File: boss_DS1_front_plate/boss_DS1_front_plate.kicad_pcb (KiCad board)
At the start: 2 copper layers, 80 x 100 mm, 16 parts

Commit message: Updated front.
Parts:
- added D1: LED, pedale:red_led, F.Cu at (74.0, 138.0)
- added D2: LED, pedale:green_led, F.Cu at (106.0, 138.0)
- added J1: top_panel_connector, pedale:bottom_connector, B.Cu at (80.5, 102.8)
- added RV1: R_Potentiometer, pedale:top_plate_pot, F.Cu at (68.0, 63.0)
- added RV2: R_Potentiometer, pedale:top_plate_pot, F.Cu at (112.0, 63.0)
- added RV3: R_Potentiometer, pedale:top_plate_pot, F.Cu at (90.0, 78.0)

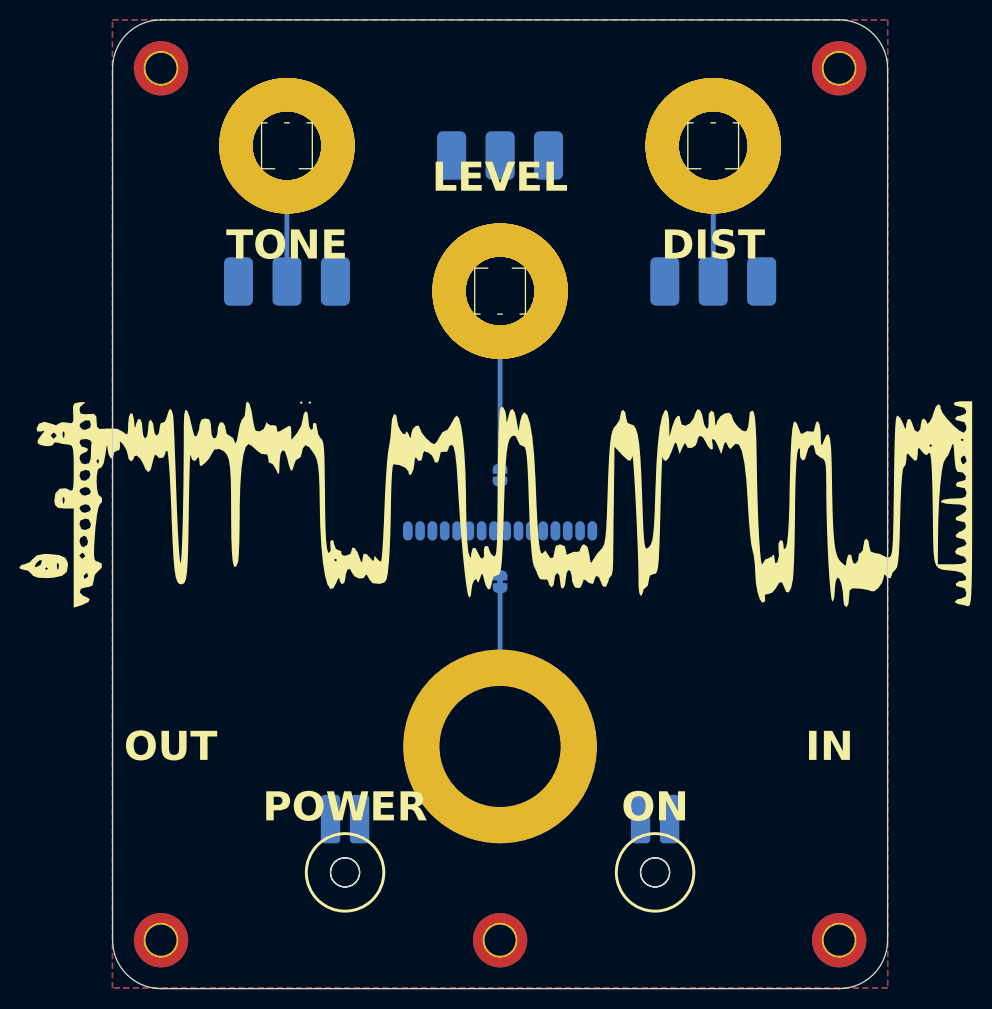
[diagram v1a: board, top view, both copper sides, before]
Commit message: Potentiometers checked.
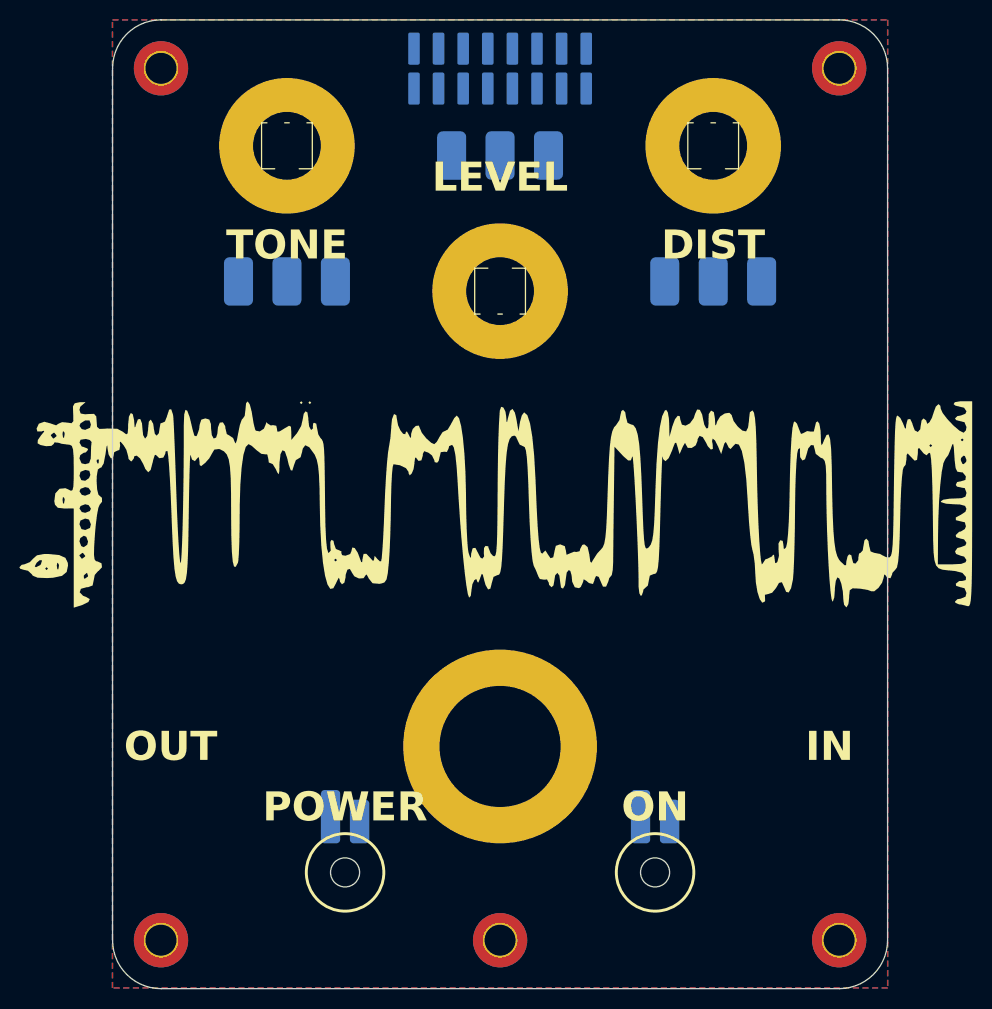
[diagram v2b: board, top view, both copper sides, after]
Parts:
- removed H10, H9: MountingHole, MountingHole:MountingHole_3mm
- removed H5, H6, H7: MountingHole_Pad, pedale:plated_pot_hole
- removed JP1, JP2, JP3, JP4: SolderJumper_2_Bridged, Jumper:SolderJumper-2_P1.3mm_Bridged_RoundedPad1.0x1.5mm
- J1: footprint pedale:bottom_connector -> pedale:IDC-Header_2x08_faux_SMD
- RV1, RV2, RV3: value R_Potentiometer -> pot_gnd
- moved J1 49.0 mm to (81.1, 53.7)
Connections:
- H8 pad 1: Net-(JP4-B) -> 0
- J1 pad 3: unconnected-(J1F-GND-Pad3) -> 0
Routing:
- net Net-(JP2-B): track 18.3 -> 0.00 mm
- net Net-(JP4-B): track 16.3 -> 0.00 mm
- net Net-(JP3-B): track 12.3 -> 0.00 mm
- net Net-(JP1-B): track 12.3 -> 0.00 mm

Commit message: Pots again, done.
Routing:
- net Net-(J1A-Pin_2): track 0.00 -> 29.5 mm
- net Net-(J1A-Pin_4): track 0.00 -> 26.4 mm
- net Net-(J1A-Pin_6): track 0.00 -> 25.4 mm
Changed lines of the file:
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@@
 	)
 	(footprint "pedale:top_plate_pot"
+		(locked yes)
 		(layer "F.Cu")
 		(at 90 78 180)
@@
 	)
 	(footprint "pedale:green_led"
+		(locked yes)
 		(layer "F.Cu")
 		(at 106 138 180)
@@
 	)
 	(footprint "pedale:top_plate_pot"
+		(locked yes)
 		(layer "F.Cu")
 		(at 112 63)
@@
 	)
 	(footprint "pedale:top_plate_pot"
+		(locked yes)
 		(layer "F.Cu")
 		(at 68 63)
@@
 	)
 	(footprint "LOGO"
+		(locked yes)
 		(layer "F.Cu")
 		(at 90 100)
@@
 	)
 	(footprint "pedale:red_led"
+		(locked yes)
 		(layer "F.Cu")
 		(at 74 138 180)
@@
 	)
 	(gr_text "IN"
+		(locked yes)
 		(at 124 125 0)
 		(layer "F.SilkS")
@@
 	)
 	(gr_text "POWER\n"
+		(locked yes)
 		(at 74 133 0)
 		(layer "F.SilkS")
@@
 	)
 	(gr_text "OUT\n"
+		(locked yes)
 		(at 56 125 0)
 		(layer "F.SilkS")
@@
 	)
 	(gr_text "ON\n"
+		(locked yes)
 		(at 106 133 0)
 		(layer "F.SilkS")
@@
 		)
 	)
+	(segment
+		(start 79.1 63.297499)
+		(end 79.1 64.7)
+		(width 0.5)
+		(layer "B.Cu")
+		(net 7)
+	)
+	(segment
+		(start 68 75.8)
+		(end 68 77)
+		(width 0.5)
+		(layer "B.Cu")
+		(net 7)
+	)
+	(segment
+		(start 79.1 64.7)
+		(end 68 75.8)
+		(width 0.5)
+		(layer "B.Cu")
+		(net 7)
+	)
+	(segment
+		(start 83.65 58.747499)
+		(end 79.1 63.297499)
+		(width 0.5)
+		(layer "B.Cu")
+		(net 7)
+	)
+	(segment
+		(start 83.65 57.0925)
+		(end 83.65 58.747499)
+		(width 0.5)
+		(layer "B.Cu")
+		(net 7)
+	)
+	(segment
+		(start 86.19 57.0925)
+		(end 86.19 58.11)
+		(width 0.5)
+		(layer "B.Cu")
+		(net 12)
+	)
+	(segment
+		(start 86.19 58.11)
+		(end 80.8 63.5)
+		(width 0.5)
+		(layer "B.Cu")
+		(net 12)
+	)
+	(segment
+		(start 80.8 63.5)
+		(end 80.8 68.3)
+		(width 0.5)
+		(layer "B.Cu")
+		(net 12)
+	)
+	(segment
+		(start 73 76.1)
+		(end 73 77)
+		(width 0.5)
+		(layer "B.Cu")
+		(net 12)
+	)
+	(segment
+		(start 80.8 68.3)
+		(end 73 76.1)
+		(width 0.5)
+		(layer "B.Cu")
+		(net 12)
+	)
+	(segment
+		(start 76.8 62.4)
+		(end 76.8 65.7)
+		(width 0.5)
+		(layer "B.Cu")
+		(net 14)
+	)
+	(segment
+		(start 76.8 65.7)
+		(end 70.3 72.2)
+		(width 0.5)
+		(layer "B.Cu")
+		(net 14)
+	)
+	(segment
+		(start 81.11 58.09)
+		(end 76.8 62.4)
+		(width 0.5)
+		(layer "B.Cu")
+		(net 14)
+	)
+	(segment
+		(start 66.8 72.2)
+		(end 63 76)
+		(width 0.5)
+		(layer "B.Cu")
+		(net 14)
+	)
+	(segment
+		(start 81.11 57.0925)
+		(end 81.11 58.09)
+		(width 0.5)
+		(layer "B.Cu")
+		(net 14)
+	)
+	(segment
+		(start 70.3 72.2)
+		(end 66.8 72.2)
+		(width 0.5)
+		(layer "B.Cu")
+		(net 14)
+	)
+	(segment
+		(start 63 76)
+		(end 63 77)
+		(width 0.5)
+		(layer "B.Cu")
+		(net 14)
+	)
 	(zone

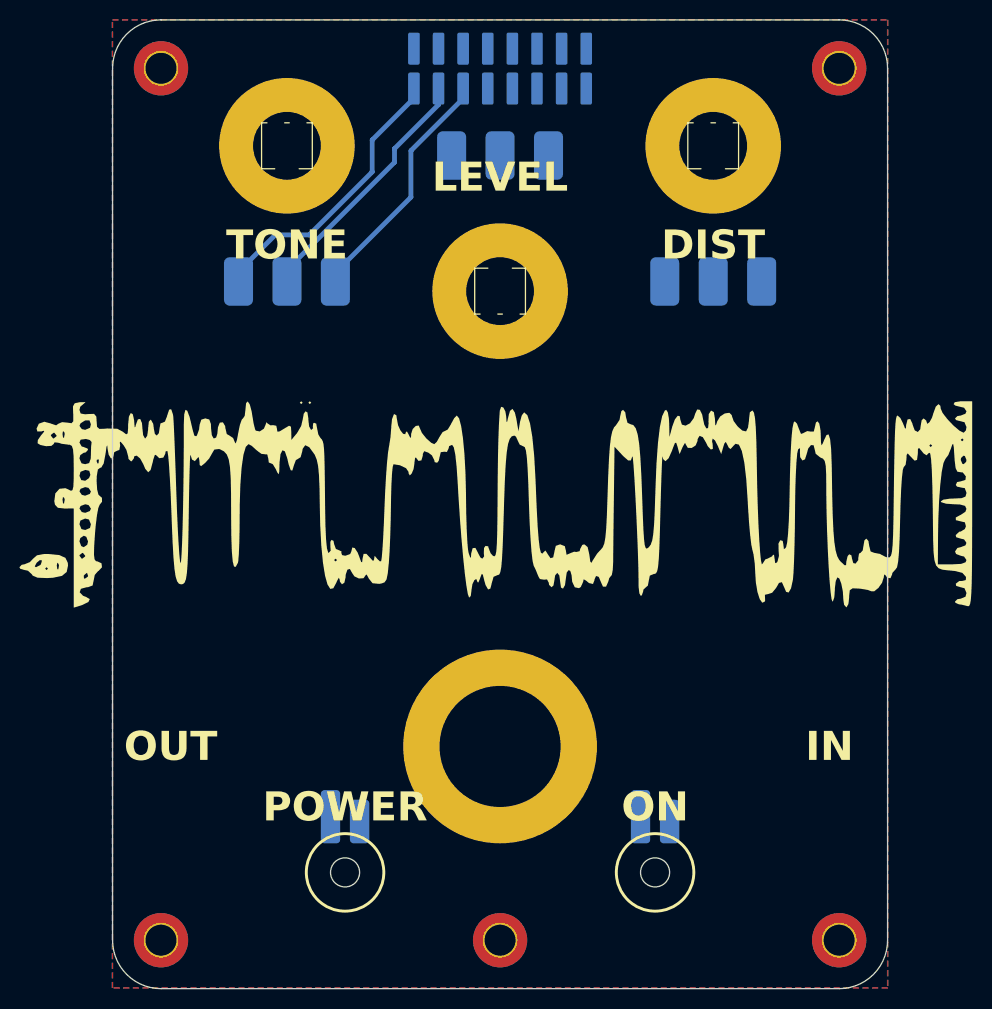
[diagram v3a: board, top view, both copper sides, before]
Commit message: Top plate routiran, valja proveriti pot-ove opet.
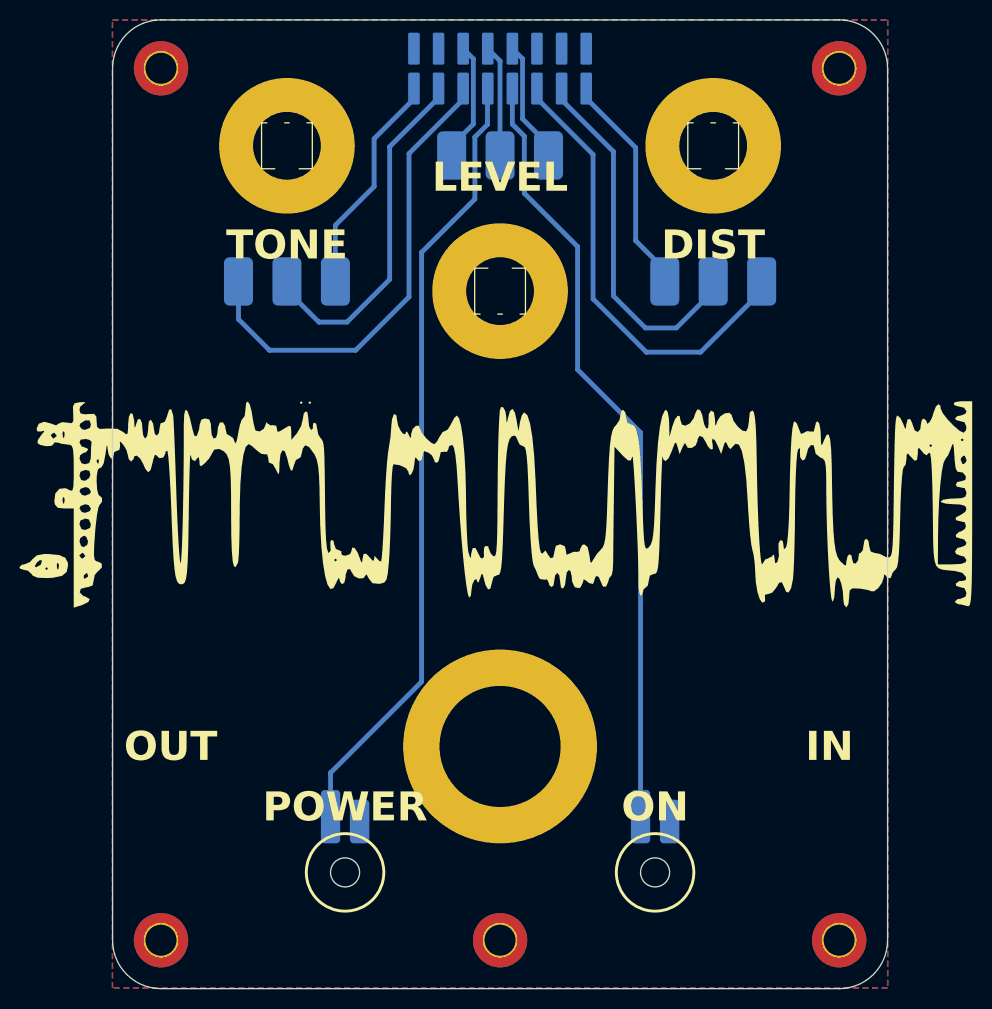
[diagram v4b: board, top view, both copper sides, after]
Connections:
- RV1 pad 1: Net-(J1A-Pin_2) -> Net-(J1A-Pin_6)
- RV1 pad 3: Net-(J1A-Pin_6) -> Net-(J1A-Pin_2)
- RV2 pad 1: Net-(J1B-Pin_5) -> Net-(J1C-Pin_16)
- RV2 pad 2: Net-(J1B-Pin_7) -> Net-(J1C-Pin_14)
- RV2 pad 3: Net-(J1B-Pin_9) -> Net-(J1C-Pin_12)
- RV3 pad 1: Net-(J1C-Pin_12) -> Net-(J1B-Pin_9)
- RV3 pad 2: Net-(J1C-Pin_14) -> Net-(J1B-Pin_7)
- RV3 pad 3: Net-(J1C-Pin_16) -> Net-(J1B-Pin_5)
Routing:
- net Net-(D1-A): track 0.00 -> 81.9 mm
- net Net-(D2-A): track 0.00 -> 80.6 mm
- net Net-(J1C-Pin_12): track 0.00 -> 47.4 mm
- net Net-(J1C-Pin_14): track 0.00 -> 37.9 mm
- net Net-(J1A-Pin_6): track 25.4 -> 49.9 mm
- net Net-(J1C-Pin_16): track 0.00 -> 23.3 mm
- net Net-(J1B-Pin_9): track 0.00 -> 12.6 mm
- net Net-(J1B-Pin_7): track 0.00 -> 11.6 mm
- net Net-(J1B-Pin_5): track 0.00 -> 11.4 mm
- net Net-(J1A-Pin_4): track 26.4 -> 36.5 mm
- net Net-(J1A-Pin_2): track 29.5 -> 23.3 mm

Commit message: Front plate update, diodes rotated.
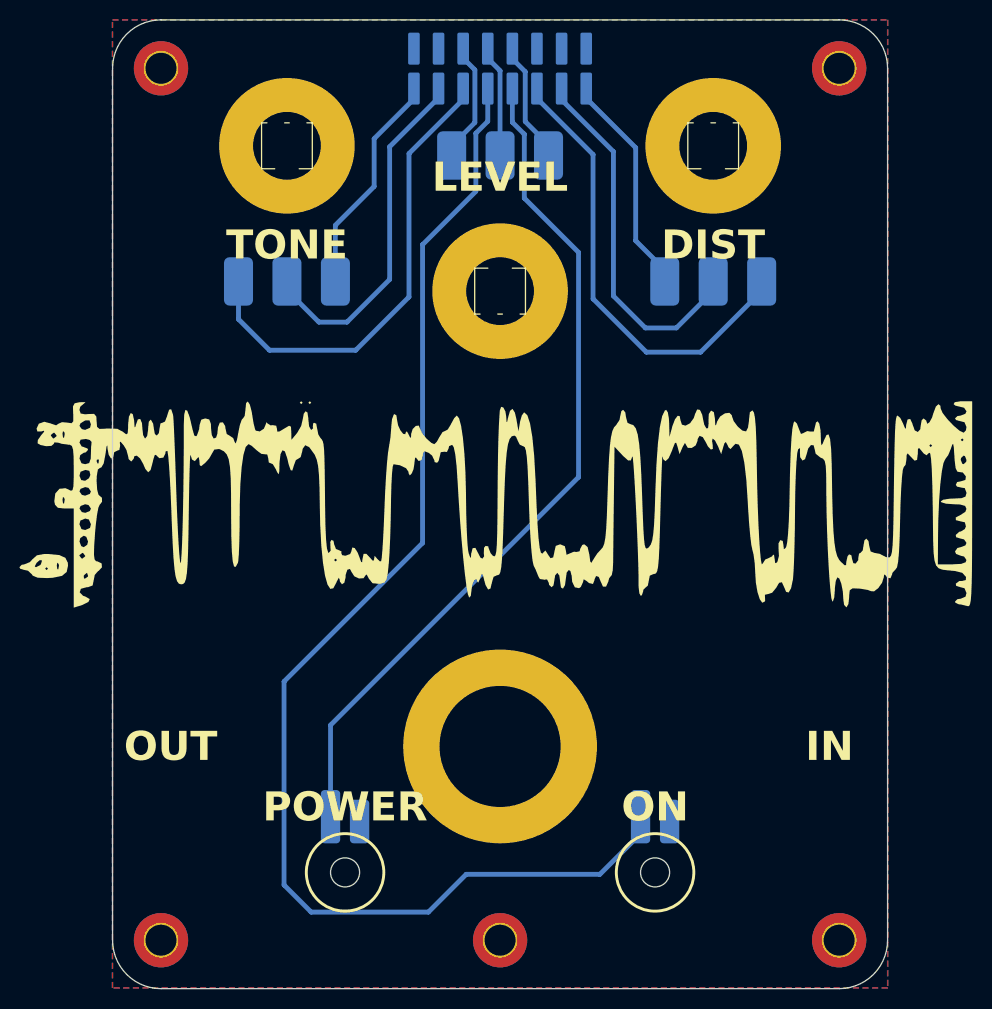
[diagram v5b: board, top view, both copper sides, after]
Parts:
- moved D1 32.0 mm to (106.0, 138.0)
- moved D2 32.0 mm to (74.0, 138.0)
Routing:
- net Net-(D1-A): track 81.9 -> 134.0 mm
- net Net-(D2-A): track 80.6 -> 88.6 mm
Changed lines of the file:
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@@
 		(locked yes)
 		(layer "F.Cu")
-		(at 106 138 180)
+		(at 74 138 180)
 		(property "Reference" "D2"
 			(at 0 -0.5 180)
@@
 		(locked yes)
 		(layer "F.Cu")
-		(at 74 138 180)
+		(at 106 138 180)
 		(property "Reference" "D1"
 			(at 0 -0.5 180)
@@
 	)
 	(segment
-		(start 87.4 68.5)
-		(end 81.9 74)
+		(start 67.7 118.3)
+		(end 67.7 139.3)
 		(width 0.5)
 		(layer "B.Cu")
@@
 	)
 	(segment
-		(start 81.9 118.320054)
-		(end 72.5 127.720054)
+		(start 82.6 142.1)
+		(end 86.5 138.2)
 		(width 0.5)
 		(layer "B.Cu")
@@
 	)
 	(segment
-		(start 81.9 74)
-		(end 81.9 118.320054)
+		(start 104.5 134)
+		(end 104.5 132.25)
 		(width 0.5)
 		(layer "B.Cu")
@@
 	)
 	(segment
-		(start 88.7 60.8)
-		(end 87.4 62.1)
+		(start 88.73 57.0925)
+		(end 88.73 60.47)
 		(width 0.5)
 		(layer "B.Cu")
@@
 	)
 	(segment
-		(start 72.5 127.720054)
-		(end 72.5 132.25)
+		(start 70.5 142.1)
+		(end 82.6 142.1)
 		(width 0.5)
 		(layer "B.Cu")
@@
 	)
 	(segment
-		(start 88.73 57.0925)
-		(end 88.7 57.1225)
+		(start 67.7 139.3)
+		(end 70.5 142.1)
+		(width 0.5)
+		(layer "B.Cu")
+		(net 2)
+	)
+	(segment
+		(start 82 73.2)
+		(end 82 104)
+		(width 0.5)
+		(layer "B.Cu")
+		(net 2)
+	)
+	(segment
+		(start 86.5 138.2)
+		(end 100.3 138.2)
+		(width 0.5)
+		(layer "B.Cu")
+		(net 2)
+	)
+	(segment
+		(start 100.3 138.2)
+		(end 104.5 134)
+		(width 0.5)
+		(layer "B.Cu")
+		(net 2)
+	)
+	(segment
+		(start 88.73 60.47)
+		(end 87.5 61.7)
+		(width 0.5)
+		(layer "B.Cu")
+		(net 2)
+	)
+	(segment
+		(start 87.5 61.7)
+		(end 87.5 67.7)
 		(width 0.5)
 		(layer "B.Cu")
@@
 	)
 	(segment
-		(start 88.7 57.1225)
-		(end 88.7 60.8)
+		(start 87.5 67.7)
+		(end 82 73.2)
 		(width 0.5)
 		(layer "B.Cu")
@@
 	)
 	(segment
-		(start 87.4 62.1)
-		(end 87.4 68.5)
+		(start 82 104)
+		(end 67.7 118.3)
 		(width 0.5)
 		(layer "B.Cu")
@@
 	)
 	(segment
-		(start 92.5 62)
-		(end 92.5 67.9)
+		(start 92.5 68.4)
+		(end 98.1 74)
 		(width 0.5)
 		(layer "B.Cu")
@@
 	)
 	(segment
-		(start 104.5 92.6)
-		(end 104.5 132.25)
+		(start 98.1 97.2)
+		(end 72.5 122.8)
 		(width 0.5)
 		(layer "B.Cu")
@@
 	)
 	(segment
-		(start 98 86.1)
-		(end 104.5 92.6)
+		(start 91.27 60.57)
+		(end 92.5 61.8)
 		(width 0.5)
 		(layer "B.Cu")
@@
 	)
 	(segment
-		(start 91.27 57.0925)
-		(end 91.27 60.77)
+		(start 92.5 61.8)
+		(end 92.5 68.4)
 		(width 0.5)
 		(layer "B.Cu")
@@
 	)
 	(segment
-		(start 92.5 67.9)
-		(end 98 73.4)
+		(start 98.1 74)
+		(end 98.1 97.2)
 		(width 0.5)
 		(layer "B.Cu")
@@
 	)
 	(segment
-		(start 98 73.4)
-		(end 98 86.1)
+		(start 91.27 57.0925)
+		(end 91.27 60.57)
 		(width 0.5)
 		(layer "B.Cu")
@@
 	)
 	(segment
-		(start 91.27 60.77)
-		(end 92.5 62)
+		(start 72.5 122.8)
+		(end 72.5 132.25)
 		(width 0.5)
 		(layer "B.Cu")
@@
 	)
 	(segment
-		(start 86.19 52.9725)
-		(end 87.241 54.0235)
+		(start 87.4 55.159)
+		(end 87.4 60.6)
 		(width 0.5)
 		(layer "B.Cu")
@@
 	)
 	(segment
-		(start 87.241 54.0235)
-		(end 87.241 60.759)
+		(start 87.4 60.6)
+		(end 85 63)
 		(width 0.5)
 		(layer "B.Cu")
@@
 	)
 	(segment
-		(start 87.241 60.759)
-		(end 85 63)
+		(start 86.19 53.949)
+		(end 87.4 55.159)
+		(width 0.5)
+		(layer "B.Cu")
+		(net 6)
+	)
+	(segment
+		(start 86.19 52.9725)
+		(end 86.19 53.949)
 		(width 0.5)
 		(layer "B.Cu")
@@
 	)
 	(segment
-		(start 92.321 54.0235)
-		(end 92.321 60.221)
+		(start 95 62.9)
+		(end 95 64)
 		(width 0.5)
 		(layer "B.Cu")
@@
 	)
 	(segment
-		(start 95 62.9)
-		(end 95 64)
+		(start 91.27 54.02125)
+		(end 92.6 55.35125)
 		(width 0.5)
 		(layer "B.Cu")
@@
 	)
 	(segment
-		(start 92.321 60.221)
+		(start 92.6 60.5)
 		(end 95 62.9)
 		(width 0.5)
@@
 	(segment
 		(start 91.27 52.9725)
-		(end 92.321 54.0235)
+		(end 91.27 54.02125)
+		(width 0.5)
+		(layer "B.Cu")
+		(net 9)
+	)
+	(segment
+		(start 92.6 55.35125)
+		(end 92.6 60.5)
 		(width 0.5)
 		(layer "B.Cu")
@@
 	)
 	(segment
+		(start 88.73 53.98)
+		(end 90 55.25)
+		(width 0.5)
+		(layer "B.Cu")
+		(net 13)
+	)
+	(segment
 		(start 88.73 52.9725)
-		(end 90 54.2425)
+		(end 88.73 53.98)
 		(width 0.5)
 		(layer "B.Cu")
@@
 	)
 	(segment
-		(start 90 54.2425)
+		(start 90 55.25)
 		(end 90 64)
 		(width 0.5)

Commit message: Added pot value label.
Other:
- board text added: "100 kOhm lin"
- board text added: "20 kOhm lin"
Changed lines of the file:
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@@
 			(at 1.27 6.1 90)
 			(layer "B.SilkS")
+			(hide yes)
 			(effects
 				(font
@@
 		)
 	)
+	(gr_text "100 kOhm lin\n"
+		(at 94.2 88.4 0)
+		(layer "B.SilkS")
+		(effects
+			(font
+				(size 1 1)
+				(thickness 0.15)
+			)
+			(justify left bottom mirror)
+		)
+	)
+	(gr_text "100 kOhm lin\n"
+		(at 118.2 83.1 0)
+		(layer "B.SilkS")
+		(effects
+			(font
+				(size 1 1)
+				(thickness 0.15)
+			)
+			(justify left bottom mirror)
+		)
+	)
+	(gr_text "20 kOhm lin\n"
+		(at 73 83 0)
+		(layer "B.SilkS")
+		(effects
+			(font
+				(size 1 1)
+				(thickness 0.15)
+			)
+			(justify left bottom mirror)
+		)
+	)
